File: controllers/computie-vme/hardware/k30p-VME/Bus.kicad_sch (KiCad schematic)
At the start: 2 parts, among them U17 VME64-P1-3R, U18 74LS148

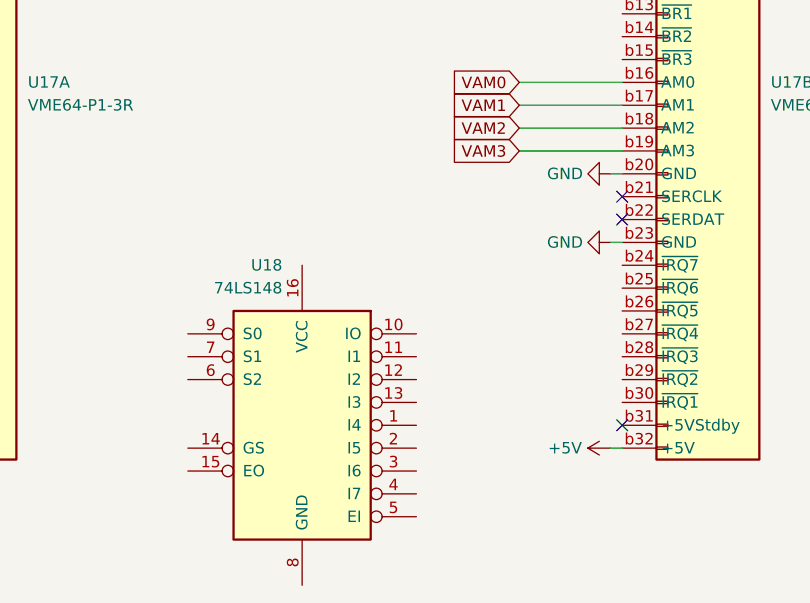
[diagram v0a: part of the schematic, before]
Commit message: Added SystemBoardSMT, renamed k30 boards, and added progress
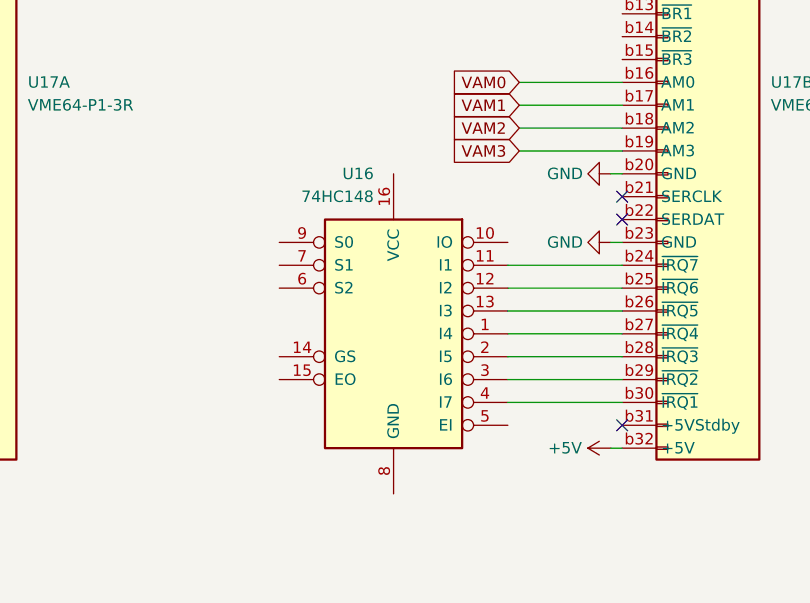
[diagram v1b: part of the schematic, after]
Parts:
- U16: renamed from U18; value 74LS148 -> 74HC148; footprint (none) -> Package_SO:SOIC-16_3.9x9.9mm_P1.27mm
- U17: footprint (none) -> Connector_DIN:DIN41612_C_3x32_Male_Horizontal_THT
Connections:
- net at U16.1 (I4): now also U17.b27 (~{IRQ4})
- net at U16.11 (I1): now also U17.b24 (~{IRQ7})
- net at U16.12 (I2): now also U17.b25 (~{IRQ6})
- net at U16.13 (I3): now also U17.b26 (~{IRQ5})
- net at U16.2 (I5): now also U17.b28 (~{IRQ3})
- net at U16.3 (I6): now also U17.b29 (~{IRQ2})
- net at U16.4 (I7): now also U17.b30 (~{IRQ1})
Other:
- moved on the sheet: U16
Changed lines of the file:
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@@
 	(wire
 		(pts
+			(xy 140.97 85.09) (xy 153.67 85.09)
+		)
+		(stroke
+			(width 0)
+			(type default)
+		)
+	)
+	(wire
+		(pts
 			(xy 68.58 44.45) (xy 68.58 49.53)
 		)
@@
 	(wire
 		(pts
+			(xy 140.97 90.17) (xy 153.67 90.17)
+		)
+		(stroke
+			(width 0)
+			(type default)
+		)
+	)
+	(wire
+		(pts
 			(xy 224.79 62.23) (xy 246.38 62.23)
 		)
@@
 	(wire
 		(pts
+			(xy 140.97 97.79) (xy 153.67 97.79)
+		)
+		(stroke
+			(width 0)
+			(type default)
+		)
+	)
+	(wire
+		(pts
 			(xy 245.11 102.87) (xy 246.38 102.87)
 		)
@@
 		)
 	)
+	(wire
+		(pts
+			(xy 140.97 92.71) (xy 153.67 92.71)
+		)
+		(stroke
+			(width 0)
+			(type default)
+		)
+	)
 	(bus
 		(pts
@@
 		)
 	)
+	(wire
+		(pts
+			(xy 140.97 82.55) (xy 153.67 82.55)
+		)
+		(stroke
+			(width 0)
+			(type default)
+		)
+	)
 	(bus
 		(pts
@@
 	(wire
 		(pts
+			(xy 140.97 95.25) (xy 153.67 95.25)
+		)
+		(stroke
+			(width 0)
+			(type default)
+		)
+	)
+	(wire
+		(pts
 			(xy 152.4 72.39) (xy 153.67 72.39)
 		)
@@
 		)
 	)
+	(wire
+		(pts
+			(xy 140.97 87.63) (xy 153.67 87.63)
+		)
+		(stroke
+			(width 0)
+			(type default)
+		)
+	)
 	(bus
 		(pts
@@
 				)
 			)
+			(project ""
+				(path "/dd13a6b9-cb24-4a73-96ce-c29930072fba/372c1966-b642-4e1e-8b8f-ada6fd5e1159"
+					(reference "#PWR063")
+					(unit 1)
+				)
+			)
 		)
 	)
@@
 		(on_board yes)
 		(dnp no)
-		(property "Reference" "#PWR057"
+		(property "Reference" "#PWR058"
 			(at 58.42 44.45 0)
 			(effects
@@
 			(project "IVC-k30"
 				(path "/dd13a6b9-cb24-4a73-96ce-c29930072fba/372c1966-b642-4e1e-8b8f-ada6fd5e1159"
-					(reference "#PWR057")
+					(reference "#PWR058")
 					(unit 1)
 				)
@@
 		(on_board yes)
 		(dnp no)
-		(property "Reference" "#PWR064"
+		(property "Reference" "#PWR061"
 			(at 146.05 80.01 0)
 			(effects
@@
 			(project "IVC-k30"
 				(path "/dd13a6b9-cb24-4a73-96ce-c29930072fba/372c1966-b642-4e1e-8b8f-ada6fd5e1159"
-					(reference "#PWR064")
+					(reference "#PWR061")
 					(unit 1)
 				)
@@
 	(symbol
 		(lib_id "74xx:74LS148")
-		(at 118.11 100.33 0)
+		(at 128.27 90.17 0)
 		(mirror y)
 		(unit 1)
@@
 		(on_board yes)
 		(dnp no)
-		(property "Reference" "U18"
-			(at 115.9159 82.55 0)
+		(property "Reference" "U16"
+			(at 126.0759 72.39 0)
 			(effects
 				(font
@@
 			)
 		)
-		(property "Value" "74LS148"
-			(at 115.9159 85.09 0)
+		(property "Value" "74HC148"
+			(at 126.0759 74.93 0)
 			(effects
 				(font
@@
 			)
 		)
-		(property "Footprint" ""
-			(at 118.11 100.33 0)
+		(property "Footprint" "Package_SO:SOIC-16_3.9x9.9mm_P1.27mm"
+			(at 128.27 90.17 0)
 			(effects
 				(font
@@
 		)
 		(property "Datasheet" "http://www.ti.com/lit/gpn/sn74LS148"
-			(at 118.11 100.33 0)
+			(at 128.27 90.17 0)
 			(effects
 				(font
@@
 		)
 		(property "Description" ""
-			(at 118.11 100.33 0)
+			(at 128.27 90.17 0)
 			(effects
 				(font
@@
 			(project "IVC-k30"
 				(path "/dd13a6b9-cb24-4a73-96ce-c29930072fba/372c1966-b642-4e1e-8b8f-ada6fd5e1159"
-					(reference "U18")
+					(reference "U16")
 					(unit 1)
 				)
@@
 		(on_board yes)
 		(dnp no)
-		(property "Reference" "#PWR050"
+		(property "Reference" "#PWR062"
 			(at 156.21 102.87 0)
 			(effects
@@
 			(project "IVC-k30"
 				(path "/dd13a6b9-cb24-4a73-96ce-c29930072fba/372c1966-b642-4e1e-8b8f-ada6fd5e1159"
-					(reference "#PWR050")
+					(reference "#PWR062")
 					(unit 1)
 				)
@@
 		(on_board yes)
 		(dnp no)
-		(property "Reference" "#PWR051"
+		(property "Reference" "#PWR060"
 			(at 146.05 72.39 0)
 			(effects
@@
 			(project "IVC-k30"
 				(path "/dd13a6b9-cb24-4a73-96ce-c29930072fba/372c1966-b642-4e1e-8b8f-ada6fd5e1159"
-					(reference "#PWR051")
+					(reference "#PWR060")
 					(unit 1)
 				)
@@
 		(on_board yes)
 		(dnp no)
-		(property "Reference" "#PWR048"
+		(property "Reference" "#PWR059"
 			(at 73.66 102.87 0)
 			(effects
@@
 			(project "IVC-k30"
 				(path "/dd13a6b9-cb24-4a73-96ce-c29930072fba/372c1966-b642-4e1e-8b8f-ada6fd5e1159"
-					(reference "#PWR048")
+					(reference "#PWR059")
 					(unit 1)
 				)
@@
 			)
 		)
-		(property "Footprint" ""
+		(property "Footprint" "Connector_DIN:DIN41612_C_3x32_Male_Horizontal_THT"
 			(at 158.75 21.59 0)
 			(effects
@@
 			(project "IVC-k30"
 				(path "/dd13a6b9-cb24-4a73-96ce-c29930072fba/372c1966-b642-4e1e-8b8f-ada6fd5e1159"
-					(reference "U17")
+					(reference "P3")
 					(unit 2)
 				)
@@
 			)
 		)
-		(property "Footprint" ""
+		(property "Footprint" "Connector_DIN:DIN41612_C_3x32_Male_Horizontal_THT"
 			(at 251.46 21.59 0)
 			(effects
@@
 			(project "IVC-k30"
 				(path "/dd13a6b9-cb24-4a73-96ce-c29930072fba/372c1966-b642-4e1e-8b8f-ada6fd5e1159"
-					(reference "U17")
+					(reference "P3")
 					(unit 3)
 				)
@@
 			)
 		)
-		(property "Footprint" ""
+		(property "Footprint" "Connector_DIN:DIN41612_C_3x32_Male_Horizontal_THT"
 			(at 76.2 21.59 0)
 			(effects
@@
 			(project "IVC-k30"
 				(path "/dd13a6b9-cb24-4a73-96ce-c29930072fba/372c1966-b642-4e1e-8b8f-ada6fd5e1159"
-					(reference "U17")
+					(reference "P3")
 					(unit 1)
 				)
@@
 					(unit 1)
 				)
+			)
+			(project ""
+				(path "/dd13a6b9-cb24-4a73-96ce-c29930072fba/372c1966-b642-4e1e-8b8f-ada6fd5e1159"
+					(reference "#PWR064")
+					(unit 1)
+				)

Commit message: Updating with more work in progress
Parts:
- added C12, C13, C14, C15, C16, C17, C18, C19, C20, C21, C22, C23, C24, C25, C26, C27, C28, C29, C30, C31, C32, C33: 0.1uF, Capacitor_SMD:C_0805_2012Metric_Pad1.18x1.45mm_HandSolder, symbol Device:C_Small
- added JP5: BG0IN, Connector_PinHeader_2.54mm:PinHeader_1x02_P2.54mm_Vertical, symbol Jumper:Jumper_2_Open
- added JP6: BG0OUT, Connector_PinHeader_2.54mm:PinHeader_1x02_P2.54mm_Vertical, symbol Jumper:Jumper_2_Open
- added JP7: BR0, Connector_PinHeader_2.54mm:PinHeader_1x02_P2.54mm_Vertical, symbol Jumper:Jumper_2_Open
- added U3: 74HC05, Package_SO:TSSOP-14_4.4x5mm_P0.65mm, symbol 74xx:74LS05
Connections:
- net +5V: now also U16.15 (EO), U16.16 (VCC), C12.1, C13.1, C14.1, C15.1, C16.1, C17.1, C18.1, C19.1, C20.1, C21.1, C22.1, C23.1, C24.1, C25.1, C26.1, C27.1, C28.1, C29.1, C30.1, C31.1, C32.1, C33.1
- net GND: now also U16.10 (IO), U16.14 (GS), U16.5 (EI), U16.8 (GND), C12.2, C13.2, C14.2, C15.2, C16.2, C17.2, C18.2, C19.2, C20.2, C21.2, C22.2, C23.2, C24.2, C25.2, C26.2, C27.2, C28.2, C29.2, C30.2, C31.2, C32.2, C33.2
- net ~{VBGIN}: now also JP5.1 (A)
- net ~{VBGOUT}: now also JP6.1 (A)
- net ~{VBR}: now also JP7.1 (A)
- net ~{VIACK}: now also U3.5
- net ~{VIPL2}: now reaches U16.6 (S2)
- net ~{VIPL1}: now reaches U16.7 (S1)
- net ~{VIPL0}: now reaches U16.9 (S0)
- net ~{VBR0}: now reaches U17.b12 (~{BR0})
- net ~{VBR0}: now also JP7.2 (B)
- net ~{VBG0IN}: now reaches U17.b4 (~{BG0IN})
- net ~{VBG0OUT}: now reaches U17.b5 (~{BG0OUT})
- net ~{VBG0OUT}: now also JP6.2 (B)
- net at U17.a20 (~{IACK}): now also U3.6
- net at U17.a21 (~{IACKIN}): now also U17.a22 (~{IACKOUT})
- new net ~{VB0GIN}: JP5.2 (B)
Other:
- note added: "NOTE: ONLY PERIPHERALS NEED IACKIN/IACKOUT"
- note removed: "TODO: how will interrupts work? Should you have a priority encoder on the IRQ lines?"
- title: k30-VME32 -> k30p-VME
- moved on the sheet: U16

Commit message: Reorganized a bit
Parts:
- added H1, H2: MountingHole, MountingHole:MountingHole_2.7mm_M2.5_DIN965, symbol Mechanical:MountingHole
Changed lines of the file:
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@@
+	)
+	(symbol
+		(lib_id "Mechanical:MountingHole")
+		(at 256.54 124.46 0)
+		(unit 1)
+		(exclude_from_sim no)
+		(in_bom yes)
+		(on_board yes)
+		(dnp no)
+		(fields_autoplaced yes)
+		(property "Reference" "H1"
+			(at 259.08 123.19 0)
+			(effects
+				(font
+					(size 1.27 1.27)
+				)
+				(justify left)
+			)
+		)
+		(property "Value" "MountingHole"
+			(at 259.08 125.73 0)
+			(effects
+				(font
+					(size 1.27 1.27)
+				)
+				(justify left)
+			)
+		)
+		(property "Footprint" "MountingHole:MountingHole_2.7mm_M2.5_DIN965"
+			(at 256.54 124.46 0)
+			(effects
+				(font
+					(size 1.27 1.27)
+				)
+				(hide yes)
+			)
+		)
+		(property "Datasheet" "~"
+			(at 256.54 124.46 0)
+			(effects
+				(font
+					(size 1.27 1.27)
+				)
+				(hide yes)
+			)
+		)
+		(property "Description" ""
+			(at 256.54 124.46 0)
+			(effects
+				(font
+					(size 1.27 1.27)
+				)
+				(hide yes)
+			)
+		)
+		(instances
+			(project "k30p-VME"
+				(path "/dd13a6b9-cb24-4a73-96ce-c29930072fba/372c1966-b642-4e1e-8b8f-ada6fd5e1159"
+					(reference "H1")
+					(unit 1)
+				)
+			)
+		)
 	)
 	(symbol
@@
 					(unit 1)
 				)
+			)
+		)
+	)
+	(symbol
+		(lib_id "Mechanical:MountingHole")
+		(at 256.54 132.08 0)
+		(unit 1)
+		(exclude_from_sim no)
+		(in_bom yes)
+		(on_board yes)
+		(dnp no)
+		(fields_autoplaced yes)
+		(property "Reference" "H2"
+			(at 259.08 130.81 0)
+			(effects
+				(font
+					(size 1.27 1.27)
+				)
+				(justify left)
+			)
+		)
+		(property "Value" "MountingHole"
+			(at 259.08 133.35 0)
+			(effects
+				(font
+					(size 1.27 1.27)
+				)
+				(justify left)
+			)
+		)
+		(property "Footprint" "MountingHole:MountingHole_2.7mm_M2.5_DIN965"
+			(at 256.54 132.08 0)
+			(effects
+				(font
+					(size 1.27 1.27)
+				)
+				(hide yes)
+			)
+		)
+		(property "Datasheet" "~"
+			(at 256.54 132.08 0)
+			(effects
+				(font
+					(size 1.27 1.27)
+				)
+				(hide yes)
+			)
+		)
+		(property "Description" ""
+			(at 256.54 132.08 0)
+			(effects
+				(font
+					(size 1.27 1.27)
+				)
+				(hide yes)
+			)
+		)
+		(instances
+			(project "k30p-VME"
+				(path "/dd13a6b9-cb24-4a73-96ce-c29930072fba/372c1966-b642-4e1e-8b8f-ada6fd5e1159"
+					(reference "H2")
+					(unit 1)
+				)

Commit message: Basic systemboard logic for bus arbitration is working and tested
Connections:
- net ~{VB0GIN} is gone; now on net ~{VBG0IN}: JP5.2 (B)
- net ~{VIACK}: now also U3.13; no longer U3.5
- net at U17.a20 (~{IACK}): now also U3.12; no longer U3.6
- net ~{VACFAIL}: no longer names the net of U17.b3 (~{ACFAIL})
- no-connect marks 4 -> 5
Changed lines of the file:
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@@
 	)
 	(no_connect
+		(at 153.67 29.21)
+	)
+	(no_connect
 		(at 153.67 77.47)
 	)
@@
 		)
 	)
-	(wire
-		(pts
-			(xy 142.24 29.21) (xy 153.67 29.21)
-		)
-		(stroke
-			(width 0)
-			(type default)
-		)
-	)
 	(bus
 		(pts
@@
 		)
 	)
-	(global_label "~{VB0GIN}"
+	(global_label "~{VBG0IN}"
 		(shape input)
 		(at 76.2 146.05 0)
@@
 		)
 	)
-	(global_label "~{VACFAIL}"
-		(shape input)
-		(at 142.24 29.21 180)
-		(fields_autoplaced yes)
-		(effects
-			(font
-				(size 1.27 1.27)
-			)
-			(justify right)
-		)
-		(property "Intersheetrefs" "${INTERSHEET_REFS}"
-			(at 131.9975 29.21 0)
-			(effects
-				(font
-					(size 1.27 1.27)
-				)
-				(justify right)
-				(hide yes)
-			)
-		)
-	)
 	(global_label "~{VIPL0}"
 		(shape output)
@@
 			)
 		)
-		(property "Description" ""
+		(property "Description" "Power symbol creates a global label with name \"GND\" , ground"
 			(at 64.77 44.45 0)
 			(effects
@@
 			)
 		)
-		(property "Description" ""
+		(property "Description" "Power symbol creates a global label with name \"GND\" , ground"
 			(at 152.4 80.01 0)
 			(effects
@@
 			)
 		)
-		(property "Description" ""
+		(property "Description" "Power symbol creates a global label with name \"GND\" , ground"
 			(at 194.31 158.75 0)
 			(effects
@@
 			)
 		)
-		(property "Description" ""
+		(property "Description" "Power symbol creates a global label with name \"+5V\""
 			(at 194.31 130.81 0)
 			(effects
@@
 			)
 		)
-		(property "Description" ""
+		(property "Description" "Power symbol creates a global label with name \"+5V\""
 			(at 194.31 151.13 0)
 			(effects
@@
 			)
 		)
-		(property "Description" ""
+		(property "Description" "Power symbol creates a global label with name \"+5V\""
 			(at 119.38 72.39 0)
 			(effects
@@
 			)
 		)
-		(property "Description" ""
+		(property "Description" "Power symbol creates a global label with name \"GND\" , ground"
 			(at 132.08 80.01 0)
 			(effects
@@
 			)
 		)
-		(property "Description" ""
+		(property "Description" "Power symbol creates a global label with name \"+5V\""
 			(at 152.4 102.87 0)
 			(effects
@@
 			)
 		)
-		(property "Description" ""
+		(property "Description" "Power symbol creates a global label with name \"GND\" , ground"
 			(at 152.4 72.39 0)
 			(effects
@@
 			)
 		)
-		(property "Description" ""
+		(property "Description" "Power symbol creates a global label with name \"+5V\""
 			(at 194.31 111.76 0)
 			(effects
@@
 			)
 		)
-		(property "Description" ""
+		(property "Description" "Power symbol creates a global label with name \"+5V\""
 			(at 69.85 102.87 0)
 			(effects
@@
 			)
 		)
-		(property "Description" ""
+		(property "Description" "Power symbol creates a global label with name \"+5V\""
 			(at 106.68 95.25 0)
 			(effects
@@
 			)
 		)
-		(property "Description" ""
+		(property "Description" "Power symbol creates a global label with name \"GND\" , ground"
 			(at 194.31 119.38 0)
 			(effects
@@
 		(lib_id "74xx:74LS05")
 		(at 60.96 72.39 0)
-		(unit 3)
+		(unit 6)
 		(exclude_from_sim no)
 		(in_bom yes)
@@
 				(path "/dd13a6b9-cb24-4a73-96ce-c29930072fba/372c1966-b642-4e1e-8b8f-ada6fd5e1159"
 					(reference "U3")
-					(unit 3)
+					(unit 6)
 				)
 			)
@@
 			)
 		)
-		(property "Description" ""
+		(property "Description" "Power symbol creates a global label with name \"GND\" , ground"
 			(at 132.08 100.33 0)
 			(effects
@@
 			)
 		)
-		(property "Description" ""
+		(property "Description" "Power symbol creates a global label with name \"GND\" , ground"
 			(at 194.31 138.43 0)
 			(effects
@@
 			)
 		)
-		(property "Description" ""
+		(property "Description" "Power symbol creates a global label with name \"GND\" , ground"
 			(at 106.68 92.71 0)
 			(effects
@@
 			)
 		)
-		(property "Description" ""
+		(property "Description" "Power symbol creates a global label with name \"+5V\""
 			(at 245.11 102.87 0)
 			(effects
@@
 			)
 		)
-		(property "Description" ""
+		(property "Description" "Power symbol creates a global label with name \"GND\" , ground"
 			(at 119.38 107.95 0)
 			(effects

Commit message: Schematics for k30p-VME more or less done
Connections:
- net +5V: no longer U16.15 (EO)
- net GND: no longer U16.14 (GS)
- net ~{VSYSFAIL}: no longer names the net of U17.c10 (~{SYSFAIL})
- no-connect marks 5 -> 18
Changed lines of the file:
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@@
 	)
 	(no_connect
+		(at 153.67 41.91)
+	)
+	(no_connect
 		(at 153.67 29.21)
 	)
@@
 	)
 	(no_connect
+		(at 153.67 39.37)
+	)
+	(no_connect
 		(at 71.12 100.33)
 	)
@@
 	)
 	(no_connect
+		(at 153.67 49.53)
+	)
+	(no_connect
+		(at 153.67 57.15)
+	)
+	(no_connect
+		(at 246.38 46.99)
+	)
+	(no_connect
+		(at 153.67 44.45)
+	)
+	(no_connect
+		(at 106.68 95.25)
+	)
+	(no_connect
 		(at 153.67 74.93)
 	)
+	(no_connect
+		(at 153.67 59.69)
+	)
+	(no_connect
+		(at 153.67 36.83)
+	)
+	(no_connect
+		(at 153.67 54.61)
+	)
+	(no_connect
+		(at 106.68 92.71)
+	)
+	(no_connect
+		(at 153.67 46.99)
+	)
+	(no_connect
+		(at 246.38 100.33)
+	)
 	(bus_entry
 		(at 228.6 24.13)
@@
 		)
 	)
-	(wire
-		(pts
-			(xy 242.57 46.99) (xy 246.38 46.99)
-		)
-		(stroke
-			(width 0)
-			(type default)
-		)
-	)
 	(bus
 		(pts
@@
 		)
 	)
-	(global_label "~{VSYSFAIL}"
-		(shape input)
-		(at 242.57 46.99 180)
-		(fields_autoplaced yes)
-		(effects
-			(font
-				(size 1.27 1.27)
-			)
-			(justify right)
-		)
-		(property "Intersheetrefs" "${INTERSHEET_REFS}"
-			(at 231.1785 46.99 0)
-			(effects
-				(font
-					(size 1.27 1.27)
-				)
-				(justify right)
-				(hide yes)
-			)
-		)
-	)
 	(global_label "VD[0..31]"
 		(shape bidirectional)
@@
 	)
 	(symbol
-		(lib_id "power:+5V")
-		(at 106.68 95.25 90)
-		(unit 1)
-		(exclude_from_sim no)
-		(in_bom yes)
-		(on_board yes)
-		(dnp no)
-		(property "Reference" "#PWR061"
-			(at 110.49 95.25 0)
-			(effects
-				(font
-					(size 1.27 1.27)
-				)
-				(hide yes)
-			)
-		)
-		(property "Value" "+5V"
-			(at 101.6 95.25 90)
-			(effects
-				(font
-					(size 1.27 1.27)
-				)
-			)
-		)
-		(property "Footprint" ""
-			(at 106.68 95.25 0)
-			(effects
-				(font
-					(size 1.27 1.27)
-				)
-				(hide yes)
-			)
-		)
-		(property "Datasheet" ""
-			(at 106.68 95.25 0)
-			(effects
-				(font
-					(size 1.27 1.27)
-				)
-				(hide yes)
-			)
-		)
-		(property "Description" "Power symbol creates a global label with name \"+5V\""
-			(at 106.68 95.25 0)
-			(effects
-				(font
-					(size 1.27 1.27)
-				)
-				(hide yes)
-			)
-		)
-		(pin "1"
-		)
-		(instances
-			(project "k30p-VME"
-				(path "/dd13a6b9-cb24-4a73-96ce-c29930072fba/372c1966-b642-4e1e-8b8f-ada6fd5e1159"
-					(reference "#PWR061")
-					(unit 1)
-				)
-			)
-		)
-	)
-	(symbol
 		(lib_id "Computie_Connectors:VME64-P1-3R")
 		(at 158.75 62.23 0)
@@
 					(unit 1)
 				)
-			)
-		)
-	)
-	(symbol
-		(lib_id "power:GND")
-		(at 106.68 92.71 270)
-		(unit 1)
-		(exclude_from_sim no)
-		(in_bom yes)
-		(on_board yes)
-		(dnp no)
-		(property "Reference" "#PWR060"
-			(at 100.33 92.71 0)
-			(effects
-				(font
-					(size 1.27 1.27)
-				)
-				(hide yes)
-			)
-		)
-		(property "Value" "GND"
-			(at 101.6 92.71 90)
-			(effects
-				(font
-					(size 1.27 1.27)
-				)
-			)
-		)
-		(property "Footprint" ""
-			(at 106.68 92.71 0)
-			(effects
-				(font
-					(size 1.27 1.27)
-				)
-				(hide yes)
-			)
-		)
-		(property "Datasheet" ""
-			(at 106.68 92.71 0)
-			(effects
-				(font
-					(size 1.27 1.27)
-				)
-				(hide yes)
-			)
-		)
-		(property "Description" "Power symbol creates a global label with name \"GND\" , ground"
-			(at 106.68 92.71 0)
-			(effects
-				(font
-					(size 1.27 1.27)
-				)
-				(hide yes)
-			)
-		)
-		(pin "1"
-		)
-		(instances
-			(project "k30p-VME"
-				(path "/dd13a6b9-cb24-4a73-96ce-c29930072fba/372c1966-b642-4e1e-8b8f-ada6fd5e1159"
-					(reference "#PWR060")
-					(unit 1)
-				)

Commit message: Mostly finished k30p-VME board and frontpanel
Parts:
- C25, C26, C27, C28, C29: footprint Capacitor_SMD:C_0805_2012Metric_Pad1.18x1.45mm_HandSolder -> Capacitor_SMD:C_0603_1608Metric_Pad1.08x0.95mm_HandSolder
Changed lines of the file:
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@@
 			)
 		)
-		(property "Footprint" "Capacitor_SMD:C_0805_2012Metric_Pad1.18x1.45mm_HandSolder"
+		(property "Footprint" "Capacitor_SMD:C_0603_1608Metric_Pad1.08x0.95mm_HandSolder"
 			(at 224.79 134.62 0)
 			(effects
@@
 			)
 		)
-		(property "Footprint" "Capacitor_SMD:C_0805_2012Metric_Pad1.18x1.45mm_HandSolder"
+		(property "Footprint" "Capacitor_SMD:C_0603_1608Metric_Pad1.08x0.95mm_HandSolder"
 			(at 234.95 134.62 0)
 			(effects
@@
 			)
 		)
-		(property "Footprint" "Capacitor_SMD:C_0805_2012Metric_Pad1.18x1.45mm_HandSolder"
+		(property "Footprint" "Capacitor_SMD:C_0603_1608Metric_Pad1.08x0.95mm_HandSolder"
 			(at 214.63 134.62 0)
 			(effects
@@
 			)
 		)
-		(property "Footprint" "Capacitor_SMD:C_0805_2012Metric_Pad1.18x1.45mm_HandSolder"
+		(property "Footprint" "Capacitor_SMD:C_0603_1608Metric_Pad1.08x0.95mm_HandSolder"
 			(at 234.95 115.57 0)
 			(effects
@@
 			)
 		)
-		(property "Footprint" "Capacitor_SMD:C_0805_2012Metric_Pad1.18x1.45mm_HandSolder"
+		(property "Footprint" "Capacitor_SMD:C_0603_1608Metric_Pad1.08x0.95mm_HandSolder"
 			(at 224.79 115.57 0)
 			(effects

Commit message: Added MemBird - Woodcock (16-bit VME memory card)
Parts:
- renumbered C22 to C?, C21 to C?, C13 to C?, C14 to C?, C31 to C?, C27 to C?, C30 to C?, C18 to C?, C29 to C?, C17 to C?, C33 to C?, C24 to C?, C20 to C?, C25 to C?, C28 to C?, C16 to C?, C15 to C?, C26 to C?, C23 to C?, C12 to C?, C19 to C?, C32 to C?, H1 to H?, H2 to H?, JP7 to JP?, JP5 to JP?, JP6 to JP?, U16 to U?, U3 to U?
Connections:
- net ~{VIACK}: now also U?.1; no longer U?.13
- net at U17.b10 (~{BG3IN}): now also U17.b11 (~{BG3OUT})
- net at U17.b6 (~{BG1IN}): now also U17.b7 (~{BG1OUT})
- net at U17.b8 (~{BG2IN}): now also U17.b9 (~{BG2OUT})
- net at U17.a20 (~{IACK}): now also U?.2; no longer U?.12
- no-connect marks 18 -> 12
